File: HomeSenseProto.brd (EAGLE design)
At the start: 44 x 44 mm, 18 parts, among them IC1 ESP12SMT

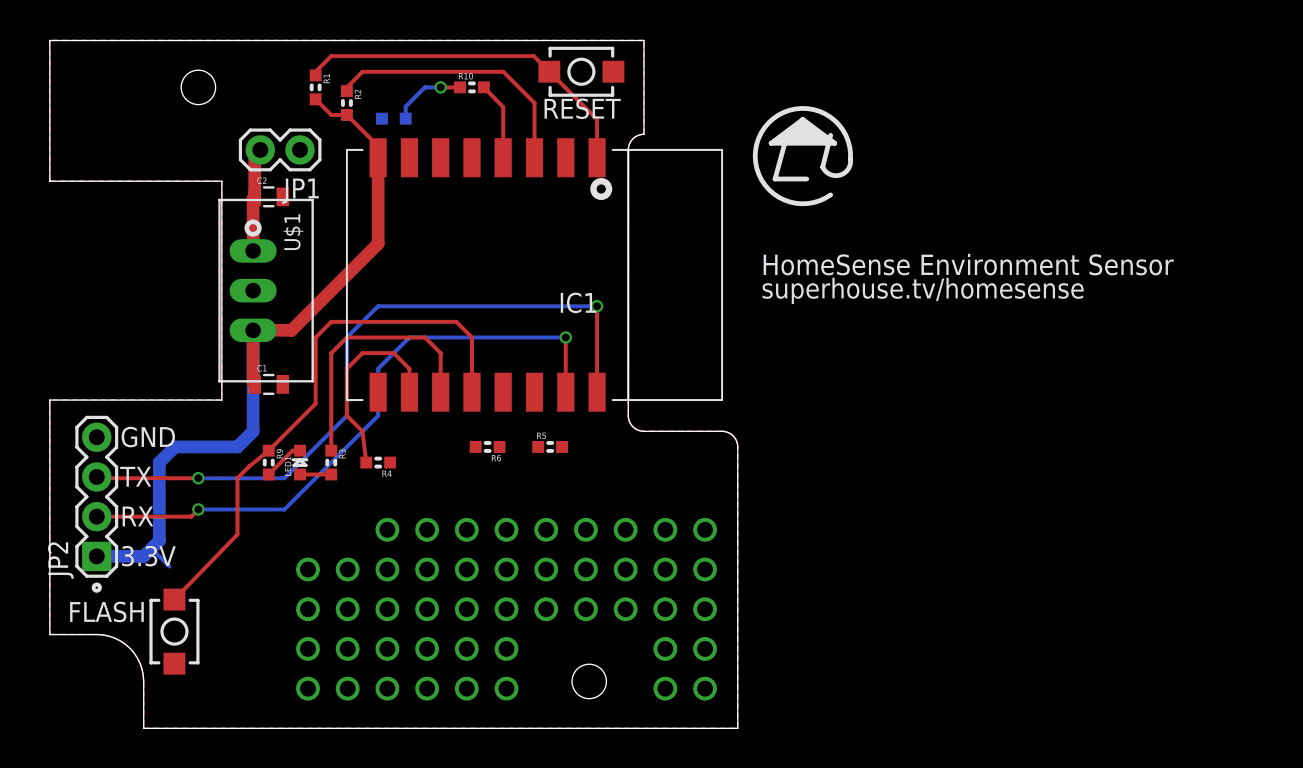
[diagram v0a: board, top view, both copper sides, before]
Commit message: Added I2C header for proto area
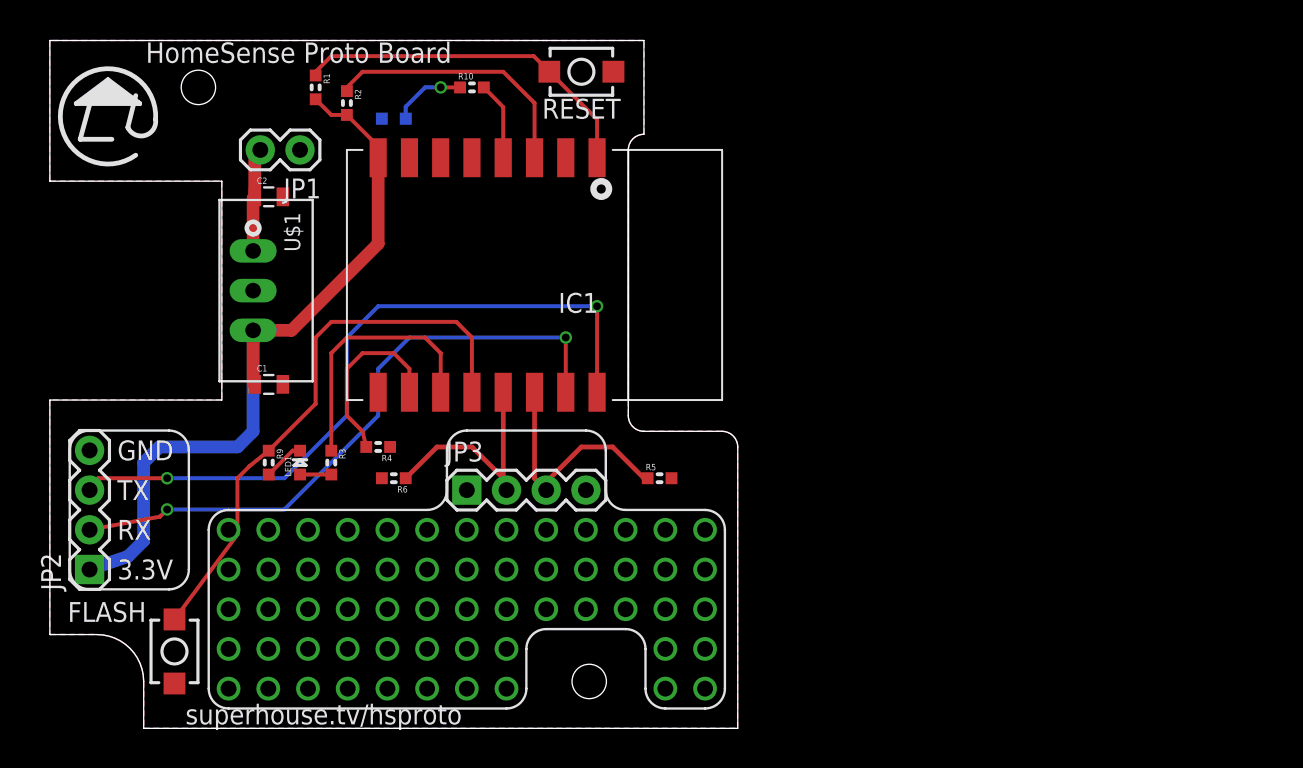
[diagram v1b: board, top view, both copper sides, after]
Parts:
- added JP3: (no value), freetronics-jon:1X04
- moved R5 7.28 mm to (39.0, 16.0)
- moved R6 6.32 mm to (22.0, 16.0)
- moved S2 1.27 mm to (7.97, 4.92)
- moved R4 1.00 mm to (21.0, 18.0)
- moved JP2 0.96 mm to (2.54, 10.2)
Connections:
- net 3.3V: now also JP3.1
- net GND: now also JP3.4
- net SCL: now also JP3.2
- net SDA: now also JP3.3
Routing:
- net SDA: track 0.00 -> 15.3 mm
- net SCL: track 0.00 -> 15.1 mm
- net 3.3V: track 51.6 -> 50.6 mm
- net GPIO15: track 12.8 -> 11.8 mm
- net GPIO0: track 34.9 -> 35.8 mm
- net TXD: track 45.0 -> 45.8 mm
- net RXD: track 40.0 -> 40.5 mm
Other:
- board text added: "HomeSense Proto Board"
- board text added: "superhouse.tv/hsproto"
- board text removed: "HomeSense Environment Sensor"
- board text removed: "superhouse.tv/homesense"

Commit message: Routing tweaks
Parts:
- added LED3: GREEN, freetronics-jon:LED-0603
- moved LED2 1.50 mm to (22.0, 40.5), flipped to the top, turned to 180 degrees
- moved R4 1.41 mm to (20.0, 17.0), turned to 90 degrees
- moved R1 1.00 mm to (17.0, 40.0)
- moved R6 1.00 mm to (22.0, 17.0), turned to 270 degrees
- moved R10 0.71 mm to (27.5, 40.5)
- renumbered U$1 to REG1
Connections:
- net GND: now also LED3.C
- net N$11: now also LED3.A
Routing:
- net 3.3V: track 50.6 -> 110.9 mm, vias 0 -> 1
- net TXD: track 45.8 -> 42.2 mm
- net GPIO0: track 35.8 -> 38.0 mm
- net RXD: track 40.5 -> 38.5 mm
- net SCL: track 15.1 -> 13.3 mm
- net SDA: track 15.3 -> 13.7 mm
- net RESET: track 22.8 -> 23.8 mm
- net N$11: track 4.75 -> 5.71 mm
- net GPIO16: track 5.01 -> 4.30 mm
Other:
- board text added: "A"
- board text added: "G"
- board text added: "HomeSense Proto"
- board text added: "IN"
- board text added: "L"
- board text added: "OUT"
- board text added: "RES"
- board text added: "SuperHouse"
- board text added: "v1.0"
- board text added: "www.superhouse.tv/hsproto"
- board text removed: "HomeSense Environmental Sensor"
- board text removed: "RESET"
- board text removed: "www.superhouse.tv/homesense"

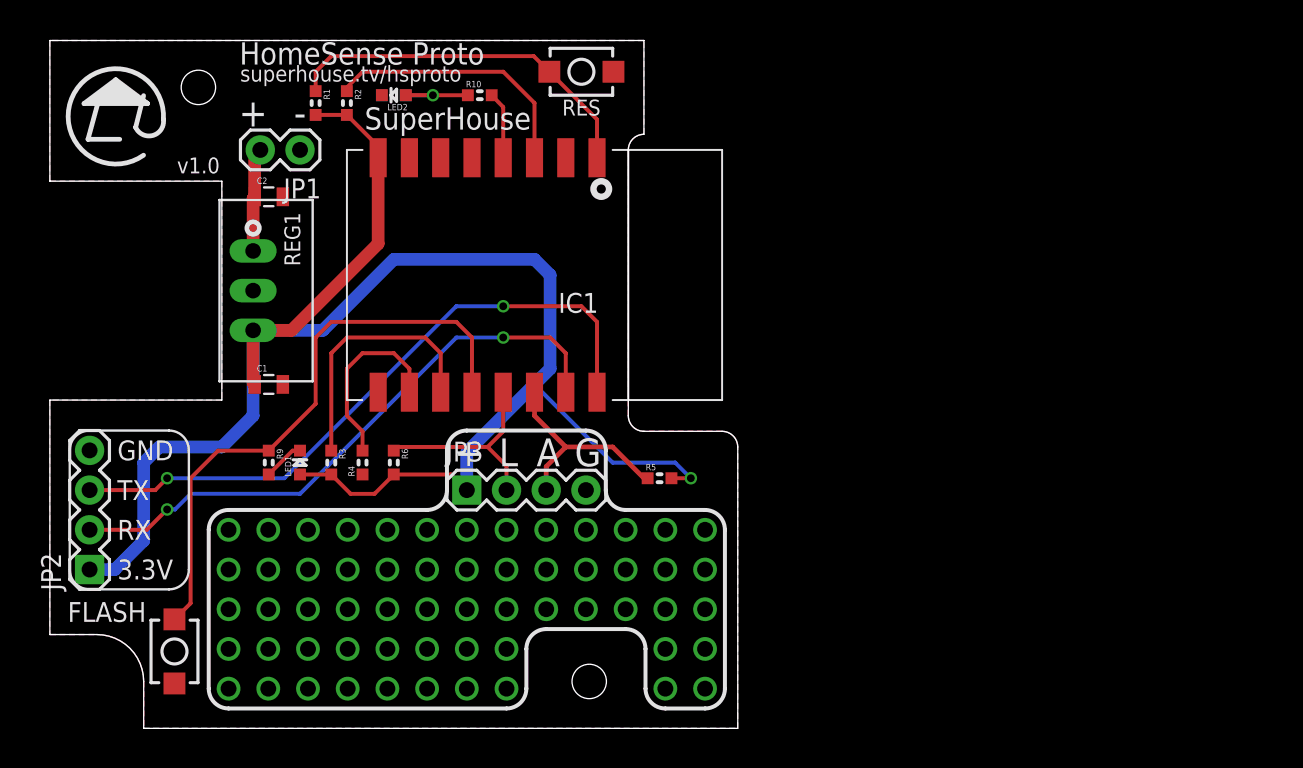
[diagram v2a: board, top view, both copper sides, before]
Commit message: Added more IO pins to breakout area
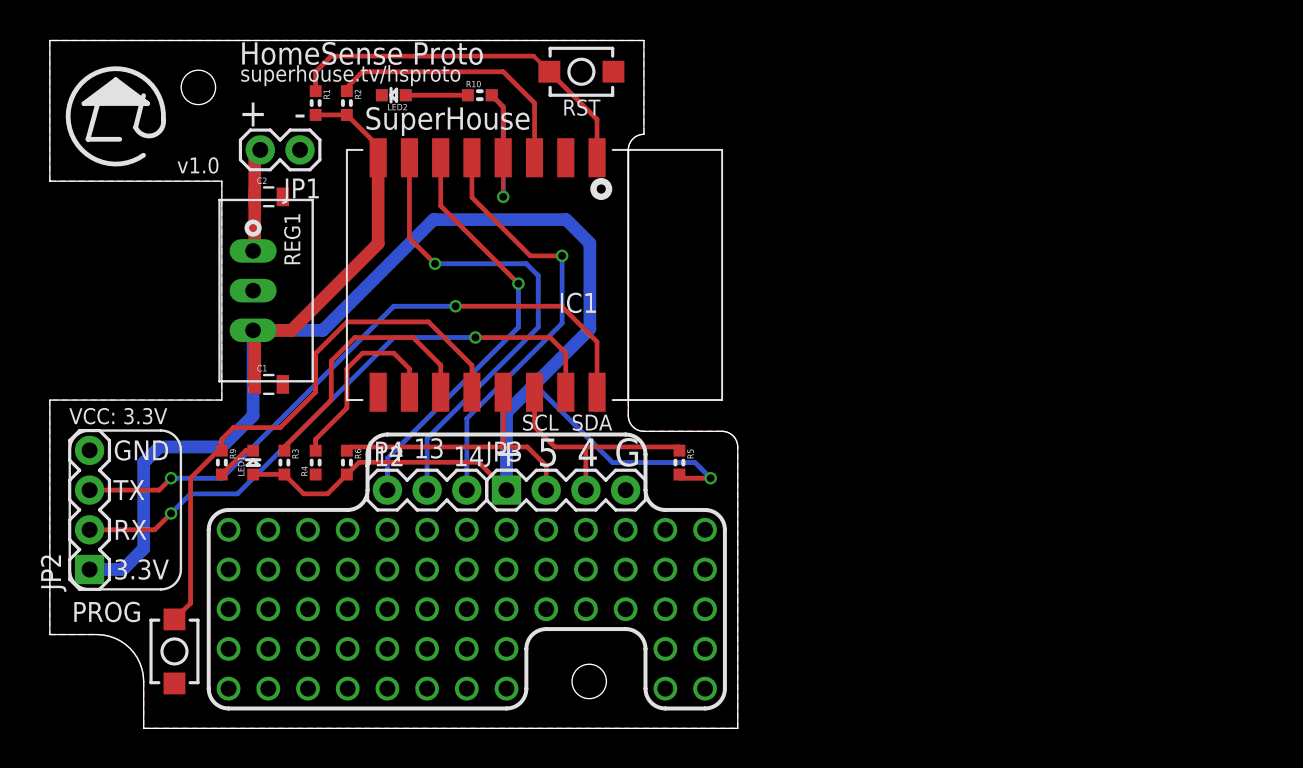
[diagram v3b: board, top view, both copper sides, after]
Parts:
- added JP4: (no value), freetronics-jon:1X03
- added R7: 1K, freetronics-jon:0603
- moved LED1 3.00 mm to (13.0, 17.0)
- moved R3 3.00 mm to (15.0, 17.0)
- moved R4 3.00 mm to (17.0, 17.0)
- moved R6 3.00 mm to (19.0, 17.0)
- moved R9 3.00 mm to (11.0, 17.0)
- moved JP3 2.54 mm to (29.2, 15.2)
- moved R5 1.62 mm to (40.3, 17.0), turned to 270 degrees
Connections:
- net SCL renamed GPIO5
- net SDA renamed GPIO4
- new net N$64: LED2.A, R10.1
- net GPIO12: now also JP4.1
- net GPIO13: now also JP4.2
- net GPIO14: now also JP4.3
- net GPIO16: now also R7.2
- net N$11: now also R7.1; no longer LED2.A, R10.1
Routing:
- net GPIO13: track 0.00 -> 31.0 mm, vias 0 -> 1
- net GPIO14: track 0.00 -> 27.4 mm, vias 0 -> 1
- net GPIO12: track 0.00 -> 26.8 mm, vias 0 -> 1
- net 3.3V: track 110.9 -> 125.5 mm
- net GPIO16: track 4.30 -> 13.6 mm, vias 0 -> 1
- net GPIO5: track 13.3 -> 18.4 mm
- net N$64: track 0.00 -> 3.98 mm
- net N$11: track 5.71 -> 3.98 mm, vias 1 -> 0
- net GPIO0: track 38.0 -> 36.3 mm
- net GPIO4: track 13.7 -> 15.0 mm
- net TXD: track 42.2 -> 41.5 mm
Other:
- board text added: "12"
- board text added: "13"
- board text added: "14"
- board text added: "4"
- board text added: "5"
- board text added: "GPIO4: SDA GPIO5: SCL"
- board text added: "PROG"
- board text added: "RST"
- board text added: "SCL"
- board text added: "SDA"
- board text added: "VCC: 3.3V"
- board text removed: "A"
- board text removed: "FLASH"
- board text removed: "HomeSense Proto Board"
- board text removed: "L"
- board text removed: "RES"

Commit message: Updated routing and schematic for v1.0 release
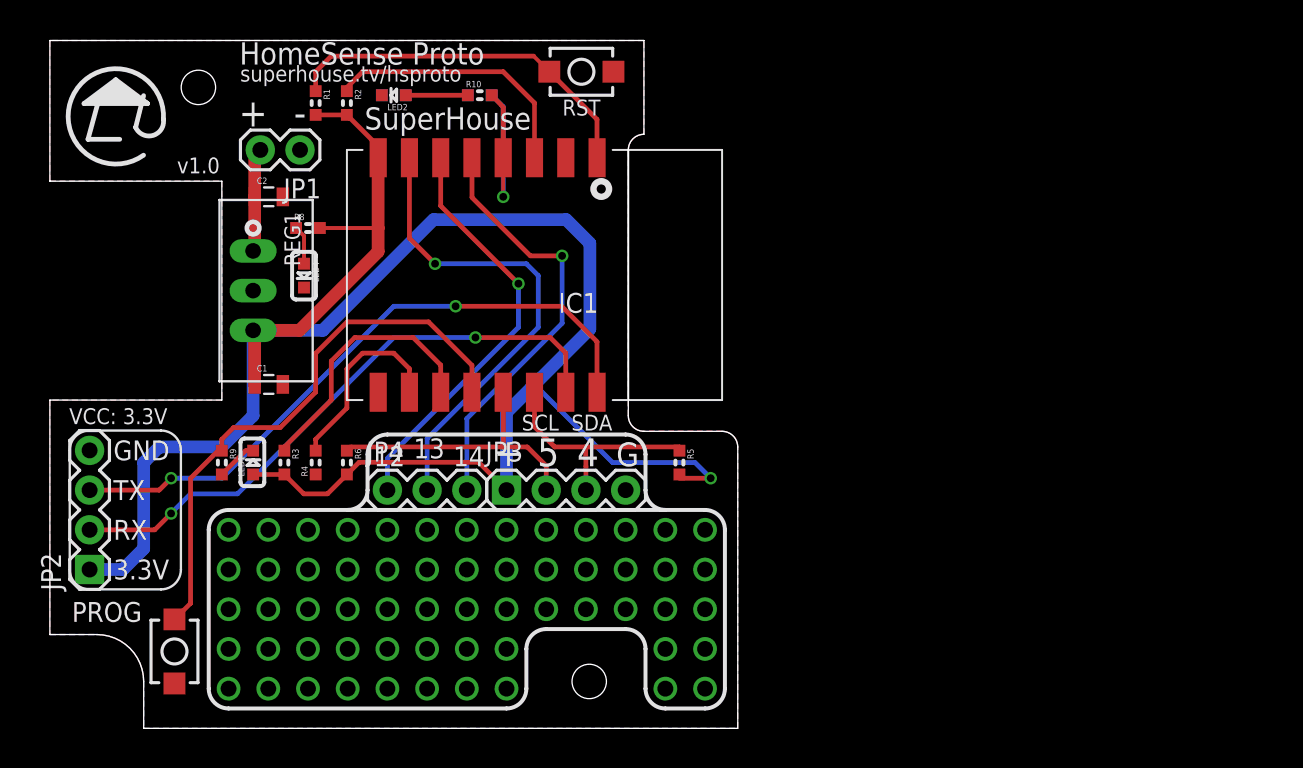
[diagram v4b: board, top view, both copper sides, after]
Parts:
- added LED4: BLUE, freetronics-jon:LED-0603
- added R8: 4K7, freetronics-jon:0603
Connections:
- new net N$65: LED4.A, R8.1
- net 3.3V: now also R8.2
- net GND: now also LED4.C
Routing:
- net 3.3V: track 125.5 -> 129.5 mm
- net N$65: track 0.00 -> 2.50 mm
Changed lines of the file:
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@@
 <hole x="9.5" y="41" drill="2.2"/>
 <text x="37" y="41.5" size="1.778" layer="22" font="vector" ratio="18" rot="MR0">HomeSense Proto</text>
-<text x="37" y="38.5" size="0.9" layer="22" font="vector" ratio="12" rot="MR0">www.superhouse.tv/hsproto</text>
+<text x="37" y="38.5" size="0.9" layer="22" font="vector" ratio="16" rot="MR0">www.superhouse.tv/hsproto</text>
 <wire x1="7.264" y1="38.95" x2="5.994" y2="36.664" width="0.3048" layer="21" curve="309.2564"/>
 <wire x1="7.264" y1="38.95" x2="5.486" y2="38.442" width="0.3048" layer="21" curve="-163.361194"/>
@@
 <text x="4.064" y="12.065" size="1.27" layer="21" font="vector" ratio="14">RX</text>
 <text x="4.064" y="9.525" size="1.27" layer="21" font="vector" ratio="14">3.3V</text>
-<text x="3.65" y="6.81" size="1.27" layer="21" font="vector" align="bottom-center">PROG</text>
-<text x="34" y="39.2" size="1.016" layer="21" font="vector" align="bottom-center">RST</text>
+<text x="3.65" y="6.81" size="1.27" layer="21" font="vector" ratio="16" align="bottom-center">PROG</text>
+<text x="34" y="39.2" size="1.016" layer="21" font="vector" ratio="16" align="bottom-center">RST</text>
 <text x="13" y="38" size="1.6764" layer="22" font="vector" ratio="16" rot="MR0" align="bottom-center">+</text>
 <text x="16" y="38" size="1.6764" layer="22" font="vector" ratio="16" rot="MR0" align="bottom-center">-</text>
@@
 <text x="31.369" y="19.05" size="1.016" layer="21" font="vector" ratio="18" align="bottom-center">SCL</text>
 <text x="34.671" y="19.05" size="1.016" layer="21" font="vector" ratio="18" align="bottom-center">SDA</text>
-<text x="36.957" y="16.764" size="1.778" layer="21" font="vector" ratio="18" align="bottom-center">G</text>
+<text x="36.957" y="16.764" size="1.524" layer="21" font="vector" ratio="18" align="bottom-center">G</text>
 <text x="13" y="38.5" size="1.778" layer="21" font="vector" ratio="18" align="bottom-center">+</text>
 <text x="16" y="38.5" size="1.778" layer="21" font="vector" ratio="18" align="bottom-center">-</text>
@@
 <wire x1="38.1" y1="17.526" x2="38.1" y2="15.24" width="0.254" layer="22"/>
 <wire x1="38.1" y1="15.24" x2="39.37" y2="13.97" width="0.254" layer="22" curve="90"/>
-<text x="36.6522" y="16.764" size="1.778" layer="22" font="vector" ratio="18" rot="MR0" align="bottom-center">G</text>
+<text x="36.6522" y="16.764" size="1.524" layer="22" font="vector" ratio="18" rot="MR0" align="bottom-center">G</text>
 <text x="34.3662" y="19.05" size="1.016" layer="22" font="vector" ratio="18" rot="MR0" align="bottom-center">SDA</text>
 <text x="31.0642" y="19.05" size="1.016" layer="22" font="vector" ratio="18" rot="MR0" align="bottom-center">SCL</text>
@@
 <text x="28.92" y="27.842" size="1.016" layer="22" font="vector" ratio="14" rot="MR0">VCC: 3.3V</text>
 <text x="1.234" y="19.46" size="1.016" layer="21" font="vector" ratio="14">VCC: 3.3V</text>
+<wire x1="21.59" y1="13.97" x2="36.83" y2="13.97" width="0.254" layer="22"/>
+<wire x1="36.83" y1="13.97" x2="38.1" y2="15.24" width="0.254" layer="22" curve="90"/>
+<wire x1="20.32" y1="15.24" x2="21.59" y2="13.97" width="0.254" layer="22" curve="90"/>
+<wire x1="36.83" y1="13.97" x2="39.37" y2="13.97" width="0.254" layer="22"/>
+<wire x1="19.05" y1="13.97" x2="21.59" y2="13.97" width="0.254" layer="22"/>
+<wire x1="19.05" y1="13.97" x2="39.37" y2="13.97" width="0.254" layer="21"/>
+<wire x1="15.748" y1="30.48" x2="15.494" y2="30.226" width="0.254" layer="21" curve="90"/>
+<wire x1="15.494" y1="30.226" x2="15.494" y2="27.686" width="0.254" layer="21"/>
+<wire x1="15.494" y1="27.686" x2="15.748" y2="27.432" width="0.254" layer="21" curve="90"/>
+<wire x1="15.748" y1="27.432" x2="16.764" y2="27.432" width="0.254" layer="21"/>
+<wire x1="16.764" y1="27.432" x2="17.018" y2="27.686" width="0.254" layer="21" curve="90"/>
+<wire x1="17.018" y1="27.686" x2="17.018" y2="30.226" width="0.254" layer="21"/>
+<wire x1="17.018" y1="30.226" x2="16.764" y2="30.48" width="0.254" layer="21" curve="90"/>
+<wire x1="16.764" y1="30.48" x2="15.748" y2="30.48" width="0.254" layer="21"/>
+<wire x1="12.446" y1="18.542" x2="12.192" y2="18.288" width="0.254" layer="21" curve="90"/>
+<wire x1="12.192" y1="18.288" x2="12.192" y2="15.748" width="0.254" layer="21"/>
+<wire x1="12.192" y1="15.748" x2="12.446" y2="15.494" width="0.254" layer="21" curve="90"/>
+<wire x1="12.446" y1="15.494" x2="13.462" y2="15.494" width="0.254" layer="21"/>
+<wire x1="13.462" y1="15.494" x2="13.716" y2="15.748" width="0.254" layer="21" curve="90"/>
+<wire x1="13.716" y1="15.748" x2="13.716" y2="18.288" width="0.254" layer="21"/>
+<wire x1="13.716" y1="18.288" x2="13.462" y2="18.542" width="0.254" layer="21" curve="90"/>
+<wire x1="13.462" y1="18.542" x2="12.446" y2="18.542" width="0.254" layer="21"/>
 </plain>
 <attributes>
@@
 <element name="R7" library="freetronics-jon" package="0603" value="1K" x="27.5" y="40.5" rot="MR180"/>
 <element name="JP4" library="freetronics-jon" package="1X03" value="" x="21.59" y="15.24"/>
+<element name="LED4" library="freetronics-jon" package="LED-0603" value="BLUE" x="16.256" y="28.956" rot="R270"/>
+<element name="R8" library="freetronics-jon" package="0603" value="4K7" x="16.51" y="32.004"/>
 </elements>
 <signals>
@@
 <contactref element="JP3" pad="4"/>
 <contactref element="LED3" pad="C"/>
+<contactref element="LED4" pad="C"/>
 </signal>
 <signal name="N$25">
@@
 <contactref element="JP2" pad="1"/>
 <contactref element="REG1" pad="3"/>
-<wire x1="13" y1="25.46" x2="15.46" y2="25.46" width="0.8128" layer="1"/>
-<wire x1="21" y1="31" x2="21" y2="36.5" width="0.8128" layer="1"/>
-<wire x1="15.46" y1="25.46" x2="21" y2="31" width="0.8128" layer="1"/>
+<wire x1="13" y1="25.46" x2="15.968" y2="25.46" width="0.8128" layer="1"/>
+<wire x1="21" y1="30.492" x2="21" y2="32.004" width="0.8128" layer="1"/>
+<wire x1="21" y1="32.004" x2="21" y2="36.5" width="0.8128" layer="1"/>
+<wire x1="15.968" y1="25.46" x2="21" y2="30.492" width="0.8128" layer="1"/>
 <wire x1="17" y1="39.238" x2="19" y2="39.238" width="0.3048" layer="1"/>
 <wire x1="19" y1="39.238" x2="21" y2="37.238" width="0.3048" layer="1"/>
@@
 <wire x1="13.1" y1="22" x2="13.1" y2="25.36" width="0.8128" layer="1"/>
 <wire x1="13.1" y1="25.36" x2="13" y2="25.46" width="0.8128" layer="1"/>
+<contactref element="R8" pad="2"/>
+<wire x1="17.272" y1="32.004" x2="21" y2="32.004" width="0.254" layer="1"/>
 </signal>
 <signal name="N$3">
@@
 <wire x1="30.734" y1="30.226" x2="27" y2="33.96" width="0.3048" layer="1"/>
 </signal>
+<signal name="N$65">
+<contactref element="R8" pad="1"/>
+<contactref element="LED4" pad="A"/>
+<wire x1="16.256" y1="29.718" x2="16.256" y2="31.496" width="0.254" layer="1"/>
+<wire x1="16.256" y1="31.496" x2="15.748" y2="32.004" width="0.254" layer="1"/>
+</signal>
 </signals>
